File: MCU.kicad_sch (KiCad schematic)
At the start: 1 part, among them U1 RP2350A

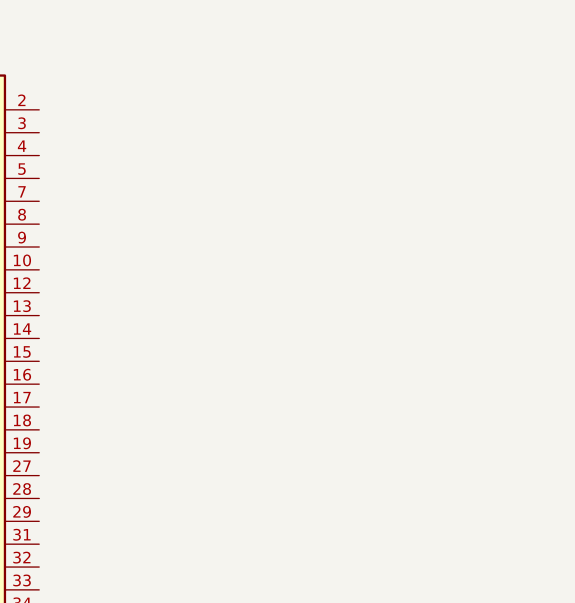
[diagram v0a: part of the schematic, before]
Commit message: Receiver design
Updated the receiver design for the SX1280.
Added an ignore for lock files.
Minor schematic updates.
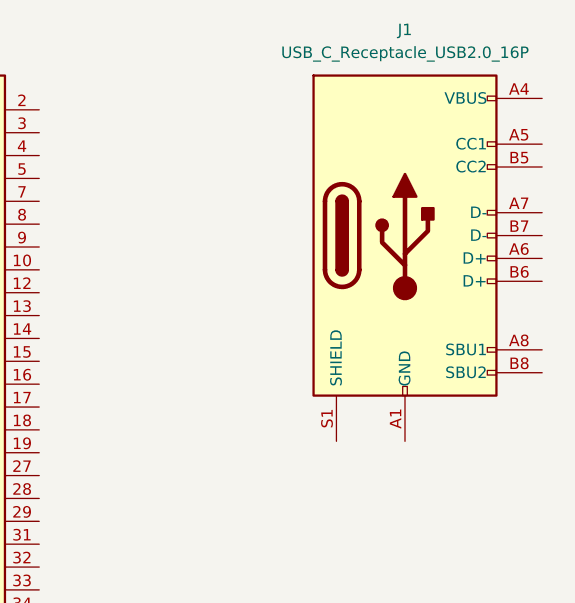
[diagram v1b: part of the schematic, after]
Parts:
- added J1: USB_C_Receptacle_USB2.0_16P, Custom_Parts:HH-16P-CB-TYPE-C, symbol Connector:USB_C_Receptacle_USB2.0_16P
- U1: footprint Package_DFN_QFN:QFN-60-1EP_7x7mm_P0.4mm_EP3.4x3.4mm -> Custom_Parts:RP2350A_QFN-60_EP_7.75x7.75_Pitch0.4mm
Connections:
- new net: J1.A1 (GND), J1.A12 (GND), J1.B1 (GND), J1.B12 (GND)
- new net: J1.A4 (VBUS), J1.A9 (VBUS), J1.B4 (VBUS), J1.B9 (VBUS)
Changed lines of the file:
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@@
+	)
+	(symbol
+		(lib_id "Connector:USB_C_Receptacle_USB2.0_16P")
+		(at 147.32 71.12 0)
+		(unit 1)
+		(exclude_from_sim no)
+		(in_bom yes)
+		(on_board yes)
+		(dnp no)
+		(fields_autoplaced yes)
+		(property "Reference" "J1"
+			(at 147.32 48.26 0)
+			(effects
+				(font
+					(size 1.27 1.27)
+				)
+			)
+		)
+		(property "Value" "USB_C_Receptacle_USB2.0_16P"
+			(at 147.32 50.8 0)
+			(effects
+				(font
+					(size 1.27 1.27)
+				)
+			)
+		)
+		(property "Footprint" "Custom_Parts:HH-16P-CB-TYPE-C"
+			(at 151.13 71.12 0)
+			(effects
+				(font
+					(size 1.27 1.27)
+				)
+				(hide yes)
+			)
+		)
+		(property "Datasheet" "https://www.usb.org/sites/default/files/documents/usb_type-c.zip"
+			(at 151.13 71.12 0)
+			(effects
+				(font
+					(size 1.27 1.27)
+				)
+				(hide yes)
+			)
+		)
+		(property "Description" "USB 2.0-only 16P Type-C Receptacle connector"
+			(at 147.32 71.12 0)
+			(effects
+				(font
+					(size 1.27 1.27)
+				)
+				(hide yes)
+			)
+		)
+		(pin "B5"
+		)
+		(pin "B8"
+		)
+		(pin "B9"
+		)
+		(pin "A7"
+		)
+		(pin "A4"
+		)
+		(pin "A1"
+		)
+		(pin "A6"
+		)
+		(pin "B1"
+		)
+		(pin "A9"
+		)
+		(pin "B6"
+		)
+		(pin "A8"
+		)
+		(pin "S1"
+		)
+		(pin "A12"
+		)
+		(pin "B4"
+		)
+		(pin "A5"
+		)
+		(pin "B12"
+		)
+		(pin "B7"
+		)
+		(instances
+			(project ""
+				(path "/ac187c6c-fa53-41cc-bce1-6f39a42a92e8/18f92408-e59e-47fb-af3d-1bd4cb05bcc2"
+					(reference "J1")
+					(unit 1)
+				)
+			)
+		)
 	)
 	(symbol
@@
 			)
 		)
-		(property "Footprint" "Package_DFN_QFN:QFN-60-1EP_7x7mm_P0.4mm_EP3.4x3.4mm"
+		(property "Footprint" "Custom_Parts:RP2350A_QFN-60_EP_7.75x7.75_Pitch0.4mm"
 			(at 81.28 95.25 0)
 			(effects

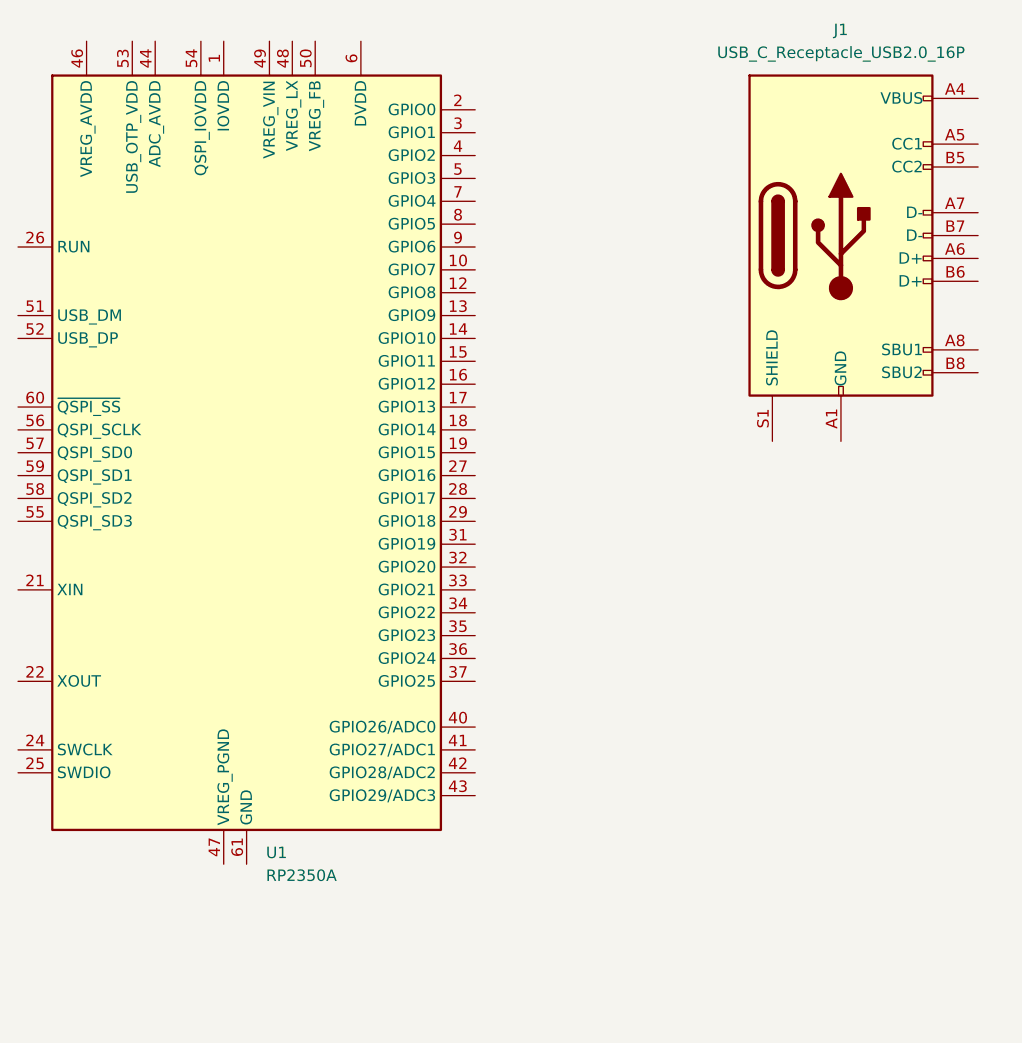
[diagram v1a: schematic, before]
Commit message: ESC design
Updated the ESC schematic.
Replaces the INA 226 with INA230.
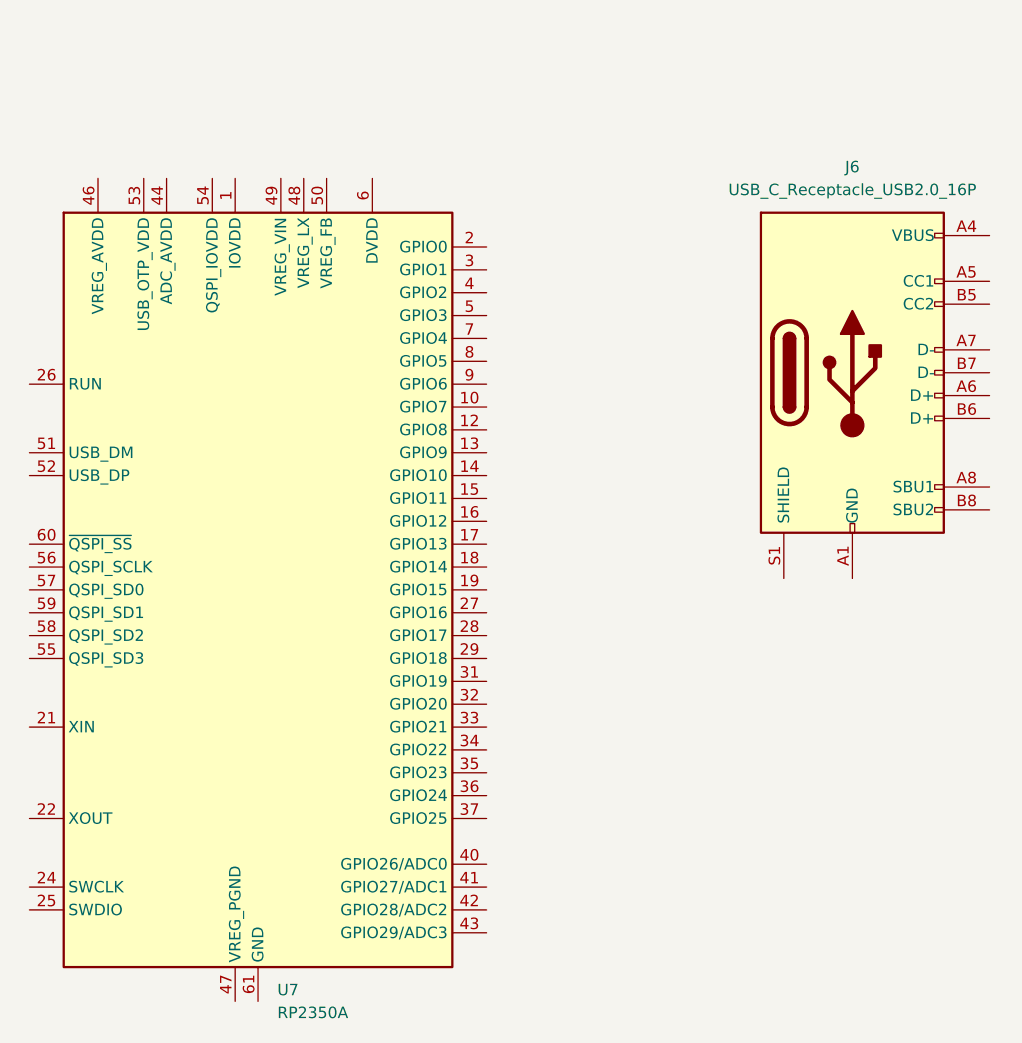
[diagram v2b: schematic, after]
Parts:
- removed J1: USB_C_Receptacle_USB2.0_16P, Custom_Parts:HH-16P-CB-TYPE-C, symbol Connector:USB_C_Receptacle_USB2.0_16P
- removed U1: RP2350A, Custom_Parts:RP2350A_QFN-60_EP_7.75x7.75_Pitch0.4mm, symbol MCU_RaspberryPi:RP2350A
- added J6: USB_C_Receptacle_USB2.0_16P, Custom_Parts:HH-16P-CB-TYPE-C, symbol Connector:USB_C_Receptacle_USB2.0_16P
- added U7: RP2350A, Custom_Parts:RP2350A_QFN-60_EP_7.75x7.75_Pitch0.4mm, symbol MCU_RaspberryPi:RP2350A
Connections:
- new net: U7.1 (IOVDD), U7.11 (IOVDD), U7.20 (IOVDD), U7.30 (IOVDD), U7.38 (IOVDD), U7.45 (IOVDD)
- new net: U7.23 (DVDD), U7.39 (DVDD), U7.6 (DVDD)
- new net: J6.A1 (GND), J6.A12 (GND), J6.B1 (GND), J6.B12 (GND)
- new net: J6.A4 (VBUS), J6.A9 (VBUS), J6.B4 (VBUS), J6.B9 (VBUS)

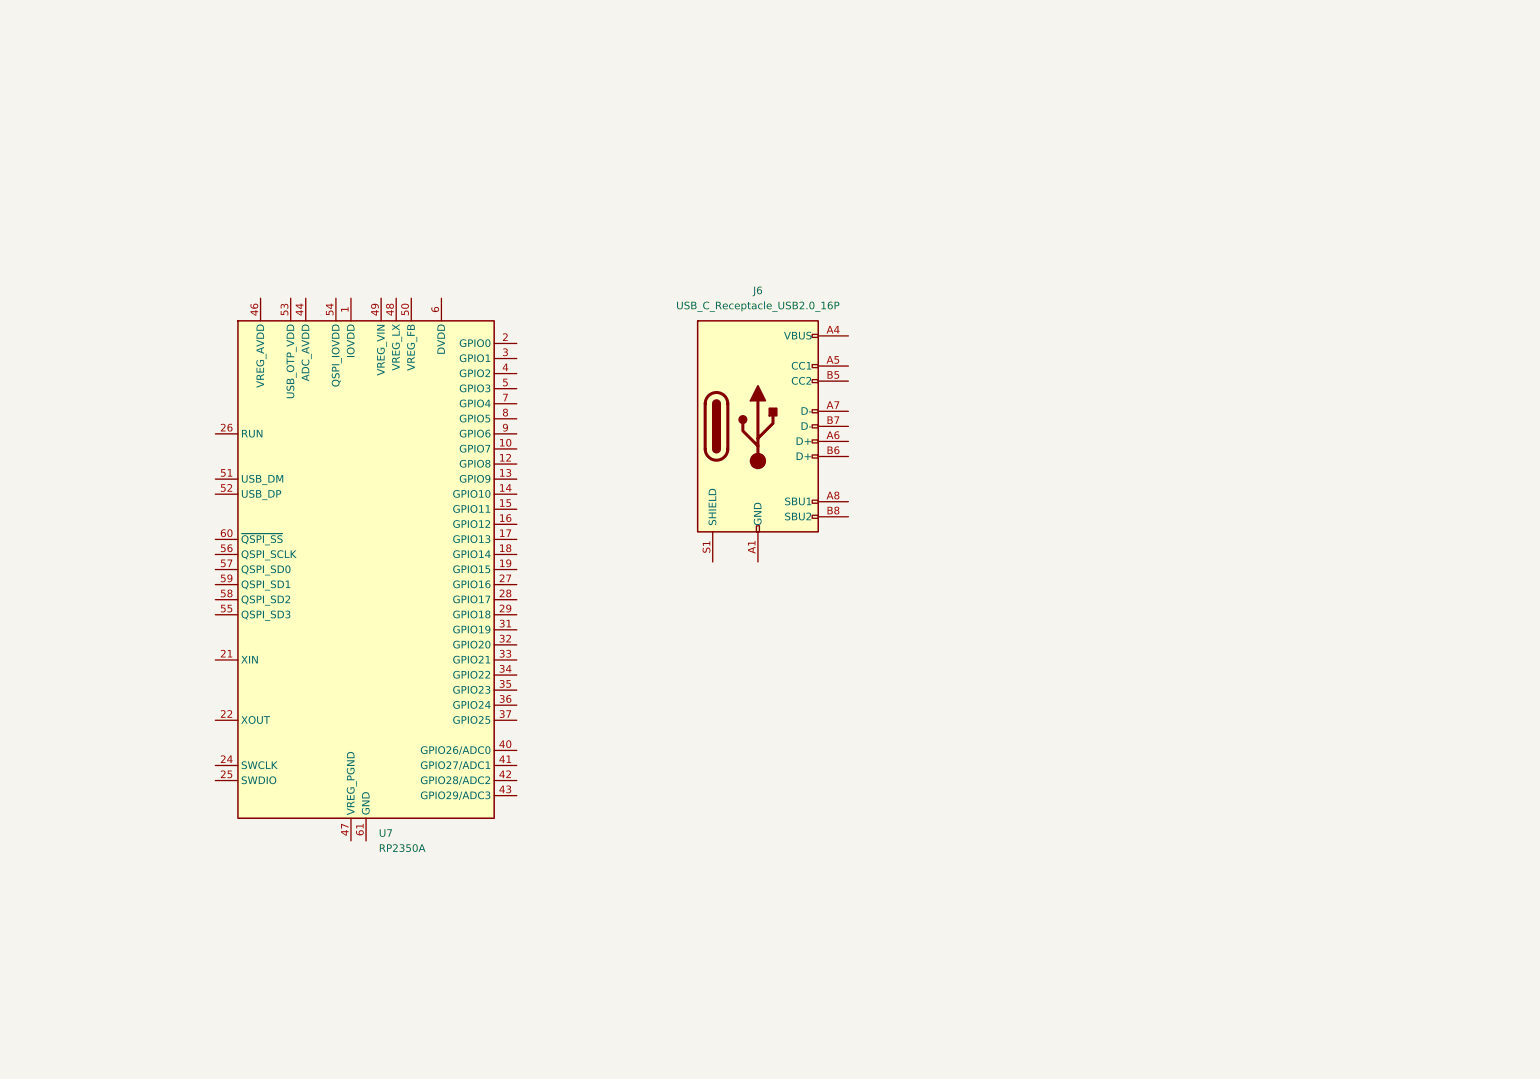
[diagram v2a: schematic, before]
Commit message: MCU design
Updated the main RP2350 schematic.
Updated labels for other designs.
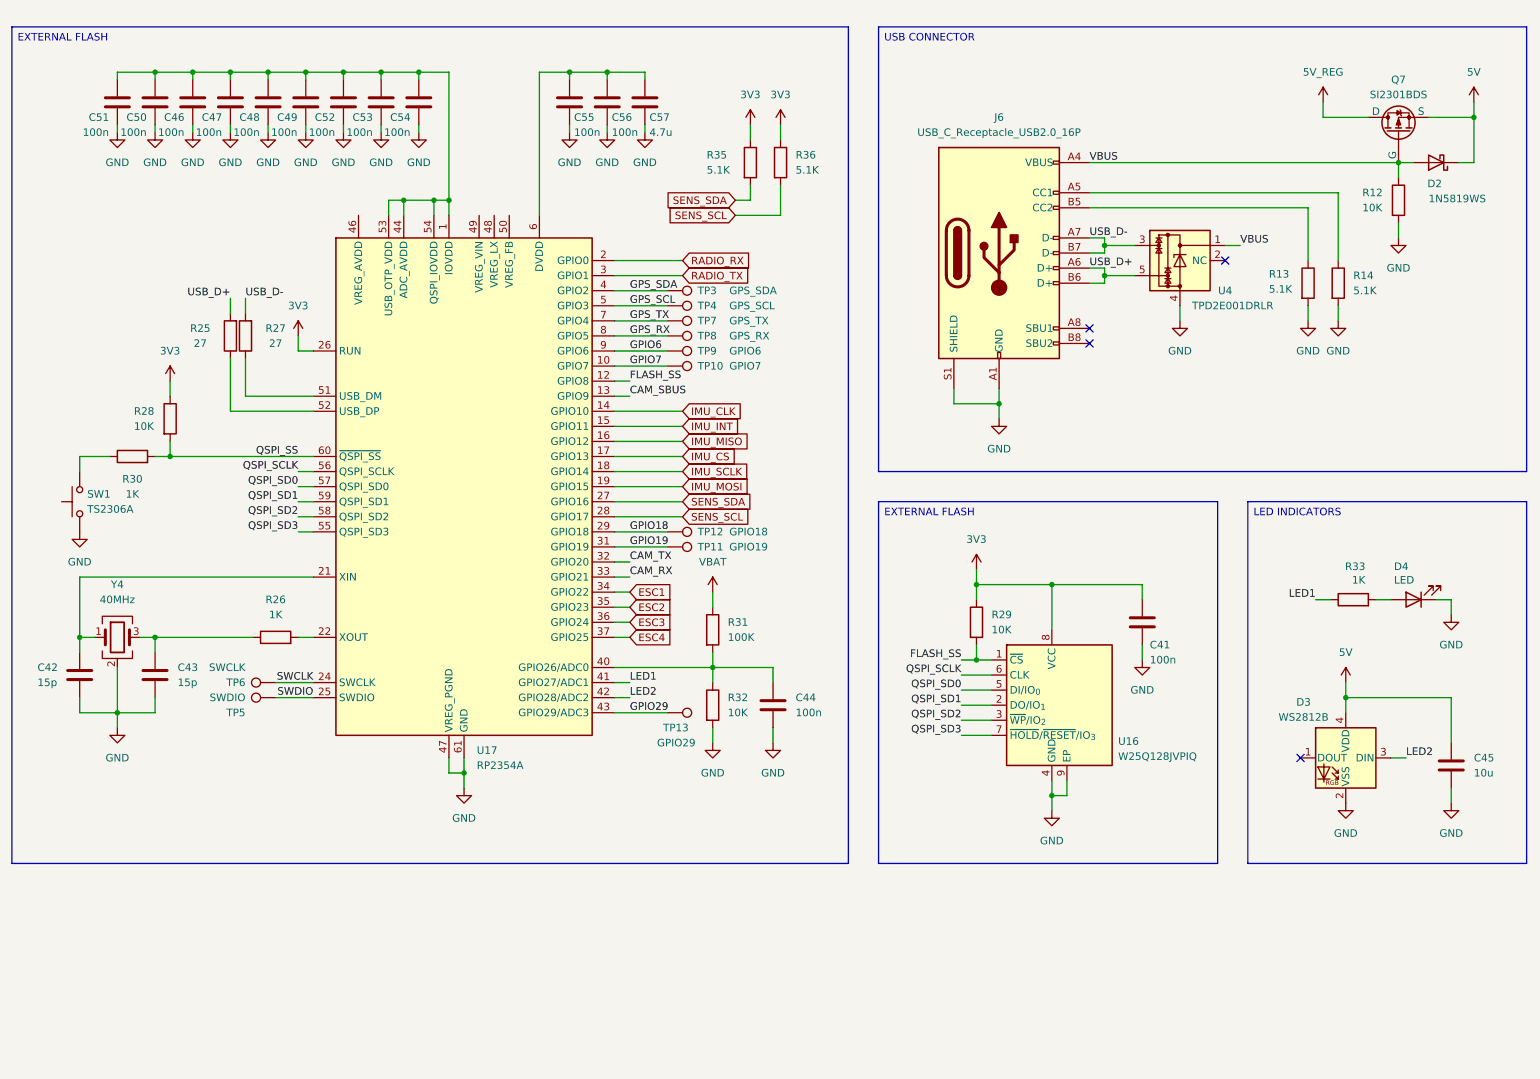
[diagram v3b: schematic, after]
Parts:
- removed U7: RP2350A, Custom_Parts:RP2350A_QFN-60_EP_7.75x7.75_Pitch0.4mm, symbol MCU_RaspberryPi:RP2350A
- added C41: 100n, Capacitor_SMD:C_0805_2012Metric, symbol Device:C
- added C42, C43: 15p, symbol Device:C
- added C44, C46, C47, C48, C49, C50, C51, C52, C53, C54, C55, C56: 100n, symbol Device:C
- added C45: 10u, symbol Device:C
- added C57: 4.7u, symbol Device:C
- added D2: 1N5819WS, Diode_SMD:D_SOD-323, symbol Diode:1N5819WS
- added D3: WS2812B, Custom_Parts:WS2812B-2020, symbol LED:WS2812B-2020
- added D4: LED, LED_SMD:LED_0805_2012Metric, symbol Device:LED
- added Q7: SI2301BDS, Package_TO_SOT_SMD:SOT-23, symbol Custom_Parts:SI2301BDS
- added R12, R28, R32: 10K, symbol Device:R
- added R13, R14, R35, R36: 5.1K, symbol Device:R
- added R25, R27: 27, symbol Device:R
- added R26, R30: 1K, symbol Device:R
- added R29: 10K, Resistor_SMD:R_0805_2012Metric, symbol Device:R
- added R31: 100K, symbol Device:R
- added R33: 1K, Resistor_SMD:R_0805_2012Metric, symbol Device:R
- added SW1: TS2306A, Custom_Parts:SW_SMD_3.0x2.0_PUSH, symbol Switch:SW_Push
- added TP10: GPIO7, TestPoint:TestPoint_Pad_D1.0mm, symbol Connector:TestPoint
- added TP11: GPIO19, TestPoint:TestPoint_Pad_D1.0mm, symbol Connector:TestPoint
- added TP12: GPIO18, TestPoint:TestPoint_Pad_D1.0mm, symbol Connector:TestPoint
- added TP13: GPIO29, TestPoint:TestPoint_Pad_D1.0mm, symbol Connector:TestPoint
- added TP3: GPS_SDA, TestPoint:TestPoint_Pad_D1.0mm, symbol Connector:TestPoint
- added TP4: GPS_SCL, TestPoint:TestPoint_Pad_D1.0mm, symbol Connector:TestPoint
- added TP5: SWDIO, TestPoint:TestPoint_Pad_D1.0mm, symbol Connector:TestPoint
- added TP6: SWCLK, TestPoint:TestPoint_Pad_D1.0mm, symbol Connector:TestPoint
- added TP7: GPS_TX, TestPoint:TestPoint_Pad_D1.0mm, symbol Connector:TestPoint
- added TP8: GPS_RX, TestPoint:TestPoint_Pad_D1.0mm, symbol Connector:TestPoint
- added TP9: GPIO6, TestPoint:TestPoint_Pad_D1.0mm, symbol Connector:TestPoint
- added U16: W25Q128JVPIQ, Package_SON:WSON-8-1EP_6x5mm_P1.27mm_EP3.4x4.3mm, symbol Memory_Flash:W25Q32JVZP
- added U17: RP2354A, Package_DFN_QFN:QFN-60-1EP_7x7mm_P0.4mm_EP3.4x3.4mm, symbol MCU_RaspberryPi:RP2354A
- added U4: TPD2E001DRLR, Package_TO_SOT_SMD:SOT-553, symbol Custom_Parts:TPD2E001DRLR
- added Y4: 40MHz, Crystal:Crystal_SMD_2016-4Pin_2.0x1.6mm, symbol Device:Crystal_GND24
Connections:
- net GND: now reaches J6.A1 (GND), J6.A12 (GND), J6.B1 (GND), J6.B12 (GND)
- net GND: now also J6.S1 (SHIELD), C41.2, C42.2, C43.2, C44.2, C45.2, C46.2, C47.2, C48.2, C49.2, C50.2, C51.2, C52.2, C53.2, C54.2, C55.2, C56.2, C57.2, D3.2 (VSS), D4.1 (K), R12.2, R13.2, R14.2, R32.2, SW1.1, U16.4 (GND), U16.9 (EP), U17.47 (VREG_PGND), U17.61 (GND), U4.4, Y4.2 (G), Y4.4 (G)
- net VBUS: now reaches J6.A4 (VBUS), J6.A9 (VBUS), J6.B4 (VBUS), J6.B9 (VBUS)
- net VBUS: now also D2.2 (A), Q7.1 (G), R12.1, U4.1
- net at J6.A5 (CC1): now also R14.1
- net USB_D+: now reaches J6.A6 (D+)
- net USB_D+: now also J6.B6 (D+), R25.2, U4.5
- net USB_D-: now reaches J6.A7 (D-)
- net USB_D-: now also J6.B7 (D-), R27.2, U4.3
- net at J6.B5 (CC2): now also R13.1
- new net: D4.2 (A), R33.2
- new net: C46.1, C47.1, C48.1, C49.1, C50.1, C51.1, C52.1, C53.1, C54.1, U17.1 (IOVDD), U17.11 (IOVDD), U17.20 (IOVDD), U17.30 (IOVDD), U17.38 (IOVDD), U17.44 (ADC_AVDD), U17.45 (IOVDD), U17.53 (USB_OTP_VDD), U17.54 (QSPI_IOVDD)
- new net: C55.1, C56.1, C57.1, U17.23 (DVDD), U17.39 (DVDD), U17.6 (DVDD)
- new net: C42.1, U17.21 (XIN), Y4.1
- new net: C43.1, R26.1, Y4.3
- new net: R26.2, U17.22 (XOUT)
- new net: R25.1, U17.52 (USB_DP)
- new net: C44.1, R31.2, R32.1, U17.40 (GPIO26/ADC0)
- new net: R27.1, U17.51 (USB_DM)
- new net: R30.1, SW1.2
- new net 3V3: C41.1, R28.1, R29.1, R35.1, R36.1, U16.8 (VCC), U17.26 (RUN)
- new net 5V: C45.1, D2.1 (K), D3.4 (VDD), Q7.2 (S)
- new net 5V_REG: Q7.3 (D)
- new net CAM_RX: U17.33 (GPIO21)
- new net CAM_SBUS: U17.13 (GPIO9)
- new net CAM_TX: U17.32 (GPIO20)
- new net ESC1: U17.34 (GPIO22)
- new net ESC2: U17.35 (GPIO23)
- new net ESC3: U17.36 (GPIO24)
- new net ESC4: U17.37 (GPIO25)
- new net FLASH_SS: R29.2, U16.1 (~{CS}), U17.12 (GPIO8)
- new net GPIO18: TP12.1, U17.29 (GPIO18)
- new net GPIO19: TP11.1, U17.31 (GPIO19)
- new net GPIO29: TP13.1, U17.43 (GPIO29/ADC3)
- new net GPIO6: TP9.1, U17.9 (GPIO6)
- new net GPIO7: TP10.1, U17.10 (GPIO7)
- new net GPS_RX: TP8.1, U17.8 (GPIO5)
- new net GPS_SCL: TP4.1, U17.5 (GPIO3)
- new net GPS_SDA: TP3.1, U17.4 (GPIO2)
- new net GPS_TX: TP7.1, U17.7 (GPIO4)
- new net IMU_CLK: U17.14 (GPIO10)
- new net IMU_CS: U17.17 (GPIO13)
- new net IMU_INT: U17.15 (GPIO11)
- new net IMU_MISO: U17.16 (GPIO12)
- new net IMU_MOSI: U17.19 (GPIO15)
- new net IMU_SCLK: U17.18 (GPIO14)
- new net LED1: R33.1, U17.41 (GPIO27/ADC1)
- new net LED2: D3.3 (DIN), U17.42 (GPIO28/ADC2)
- new net QSPI_SCLK: U16.6 (CLK), U17.56 (QSPI_SCLK)
- new net QSPI_SD0: U16.5 (DI/IO_{0}), U17.57 (QSPI_SD0)
- new net QSPI_SD1: U16.2 (DO/IO_{1}), U17.59 (QSPI_SD1)
- new net QSPI_SD2: U16.3 (~{WP}/IO_{2}), U17.58 (QSPI_SD2)
- new net QSPI_SD3: U16.7 (~{HOLD}/~{RESET}/IO_{3}), U17.55 (QSPI_SD3)
- new net QSPI_SS: R28.2, R30.2, U17.60 (~{QSPI_SS})
- new net RADIO_RX: U17.2 (GPIO0)
- new net RADIO_TX: U17.3 (GPIO1)
- new net SENS_SCL: R36.2, U17.28 (GPIO17)
- new net SENS_SDA: R35.2, U17.27 (GPIO16)
- new net SWCLK: TP6.1, U17.24 (SWCLK)
- new net SWDIO: TP5.1, U17.25 (SWDIO)
- new net VBAT: R31.1
- no-connect marks 0 -> 4
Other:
- moved on the sheet: J6
